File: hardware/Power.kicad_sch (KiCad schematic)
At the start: 28 parts, among them J1 DC Connector, Q1 DMP6180SK3-13, U1 AP66200

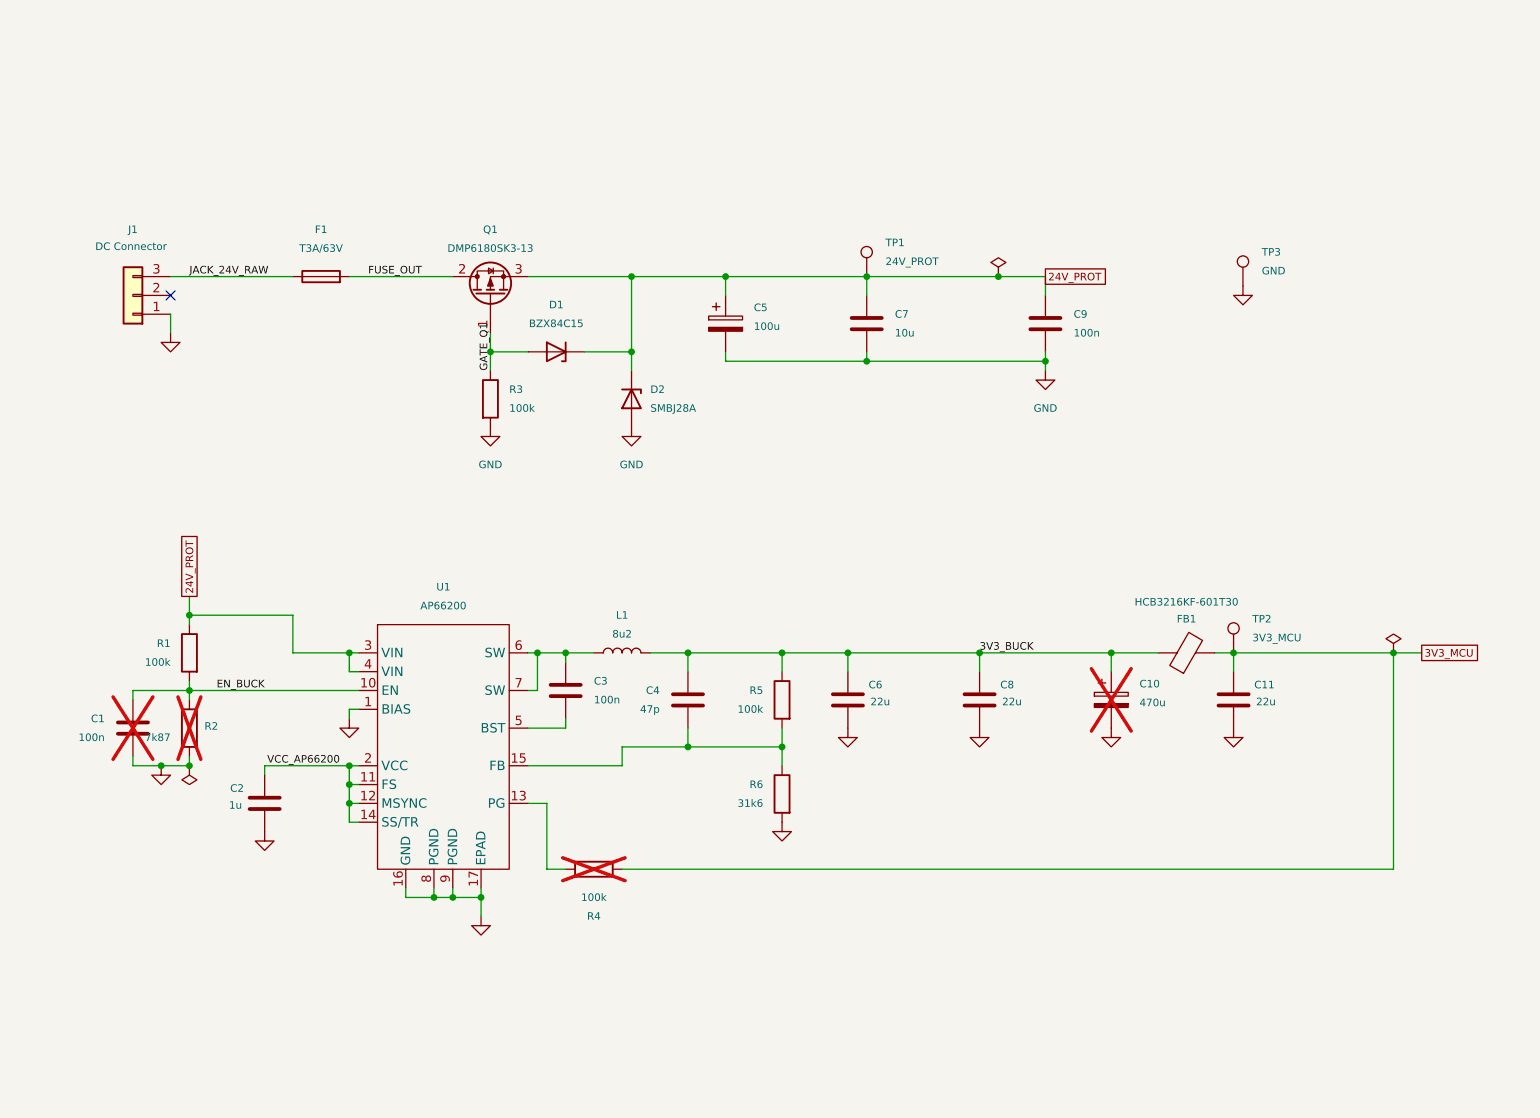
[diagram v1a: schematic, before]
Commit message: Updated power schematic, delated buck schematic
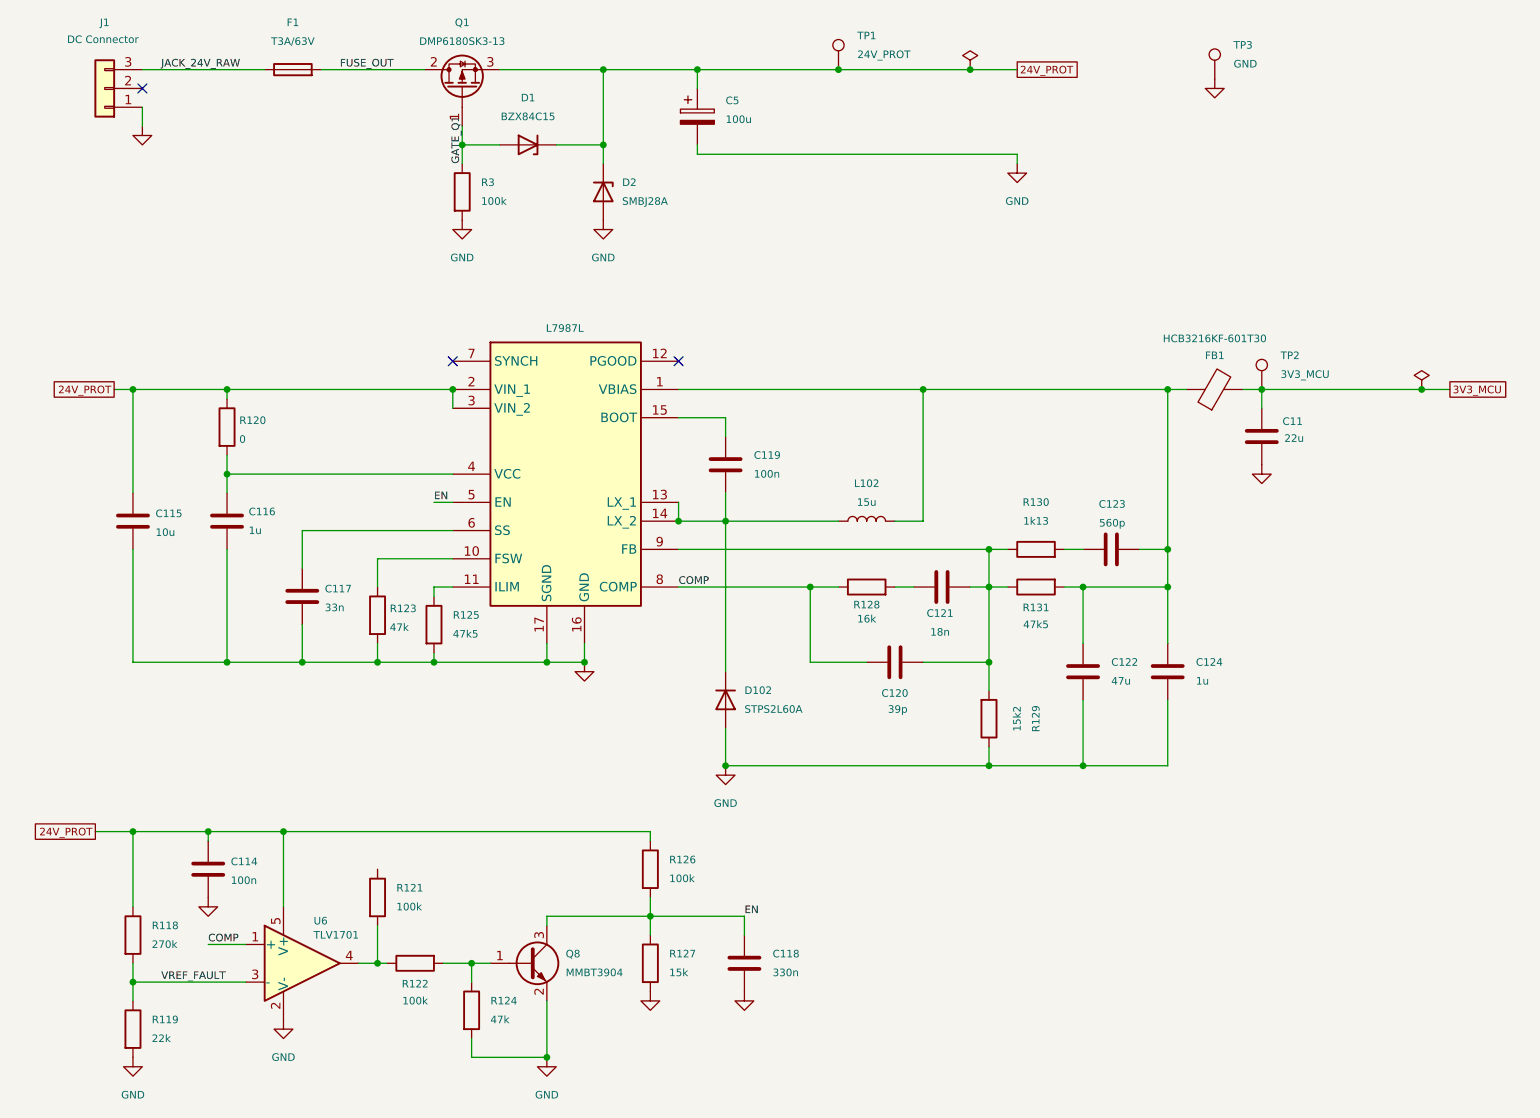
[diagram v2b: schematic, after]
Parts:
- removed C1, C3, C9: 100n, Capacitor_SMD:C_0603_1608Metric, symbol Device:C
- removed C10: 470u, Capacitor_SMD:CP_Elec_8x10, symbol Device:C_Polarized
- removed C2: 1u, Capacitor_SMD:C_0603_1608Metric, symbol Device:C
- removed C4: 47p, Capacitor_SMD:C_0603_1608Metric, symbol Device:C
- removed C6, C8: 22u, Capacitor_SMD:C_0805_2012Metric, symbol Device:C
- removed C7: 10u, Capacitor_SMD:C_1210_3225Metric, symbol Device:C
- removed L1: 8u2, JLCPCB:IND-SMD_L7.0-W6.6_ZD0650-100M, symbol Device:L
- removed R1, R4, R5: 100k, Resistor_SMD:R_0603_1608Metric, symbol Device:R
- removed R2: 7k87, Resistor_SMD:R_0603_1608Metric, symbol Device:R
- removed R6: 31k6, Resistor_SMD:R_0603_1608Metric, symbol Device:R
- removed U1: AP66200, FilamentDryer:AP66200_U-QFN4040-16_EP2.6x2.6mm_P0.65mm, symbol Filament_Dryer_Custom:AP66200
- added C114, C119: 100n, symbol Device:C
- added C115: 10u, symbol Device:C
- added C116, C124: 1u, symbol Device:C
- added C117: 33n, symbol Device:C
- added C118: 330n, symbol Device:C
- added C120: 39p, symbol Device:C
- added C121: 18n, symbol Device:C
- added C122: 47u, symbol Device:C
- added C123: 560p, symbol Device:C
- added D102: STPS2L60A, symbol Device:D
- added L102: 15u, symbol Device:L
- added Q8: MMBT3904, Package_TO_SOT_SMD:SOT-23, symbol Transistor_BJT:Q_NPN_BEC
- added R118: 270k, symbol Device:R
- added R119: 22k, symbol Device:R
- added R120: 0, symbol Device:R
- added R121, R122, R126: 100k, symbol Device:R
- added R123, R124: 47k, symbol Device:R
- added R125, R131: 47k5, symbol Device:R
- added R127: 15k, symbol Device:R
- added R128: 16k, symbol Device:R
- added R129: 15k2, symbol Device:R
- added R130: 1k13, symbol Device:R
- added U102: L7987L, SOP65P640X120-17N, symbol SamacSys_Parts:L7987L
- added U6: TLV1701, Package_TO_SOT_SMD:SOT-23-5, symbol Filament_Dryer_Custom:TLV1701AIDBVR
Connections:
- net 24V_PROT: now also C114.1, C115.1, R118.1, R120.1, R126.1, U102.2 (VIN_1), U102.3 (VIN_2), U6.5 (V+)
- net GND: now also C114.2, C115.2, C116.2, C117.2, C118.2, C122.2, C124.2, D102.2 (A), Q8.2 (E), R119.2, R123.2, R124.2, R125.2, R127.2, R129.1, U102.16 (GND), U102.17 (SGND), U6.2 (V-)
- net 3V3_BUCK: no longer names the net of FB1.1
- net 3V3_BUCK: now also C122.1, C123.2, C124.1, L102.2, R131.2, U102.1 (VBIAS)
- new net: C123.1, R130.2
- new net: Q8.1 (B), R122.2, R124.1
- new net: C121.1, R128.2
- new net: C120.2, C121.2, R129.2, R130.1, R131.1, U102.9 (FB)
- new net: R125.1, U102.11 (ILIM)
- new net: C119.1, U102.15 (BOOT)
- new net: C119.2, D102.1 (K), L102.1, U102.13 (LX_1), U102.14 (LX_2)
- new net: C116.1, R120.2, U102.4 (VCC)
- new net: R123.1, U102.10 (FSW)
- new net: C117.1, U102.6 (SS)
- new net: R121.2, R122.1, U6.4
- new net COMP: C120.1, R128.1, U102.8 (COMP), U6.1 (+)
- new net EN: C118.1, Q8.3 (C), R126.2, R127.1, U102.5 (EN)
- new net VREF_FAULT: R118.2, R119.1, U6.3 (-)
- no-connect marks 1 -> 3
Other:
- moved on the sheet: C11, C5, D1, D2, F1, FB1, J1, Q1, R3, TP1, TP2, TP3

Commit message: Updated buck circuit references
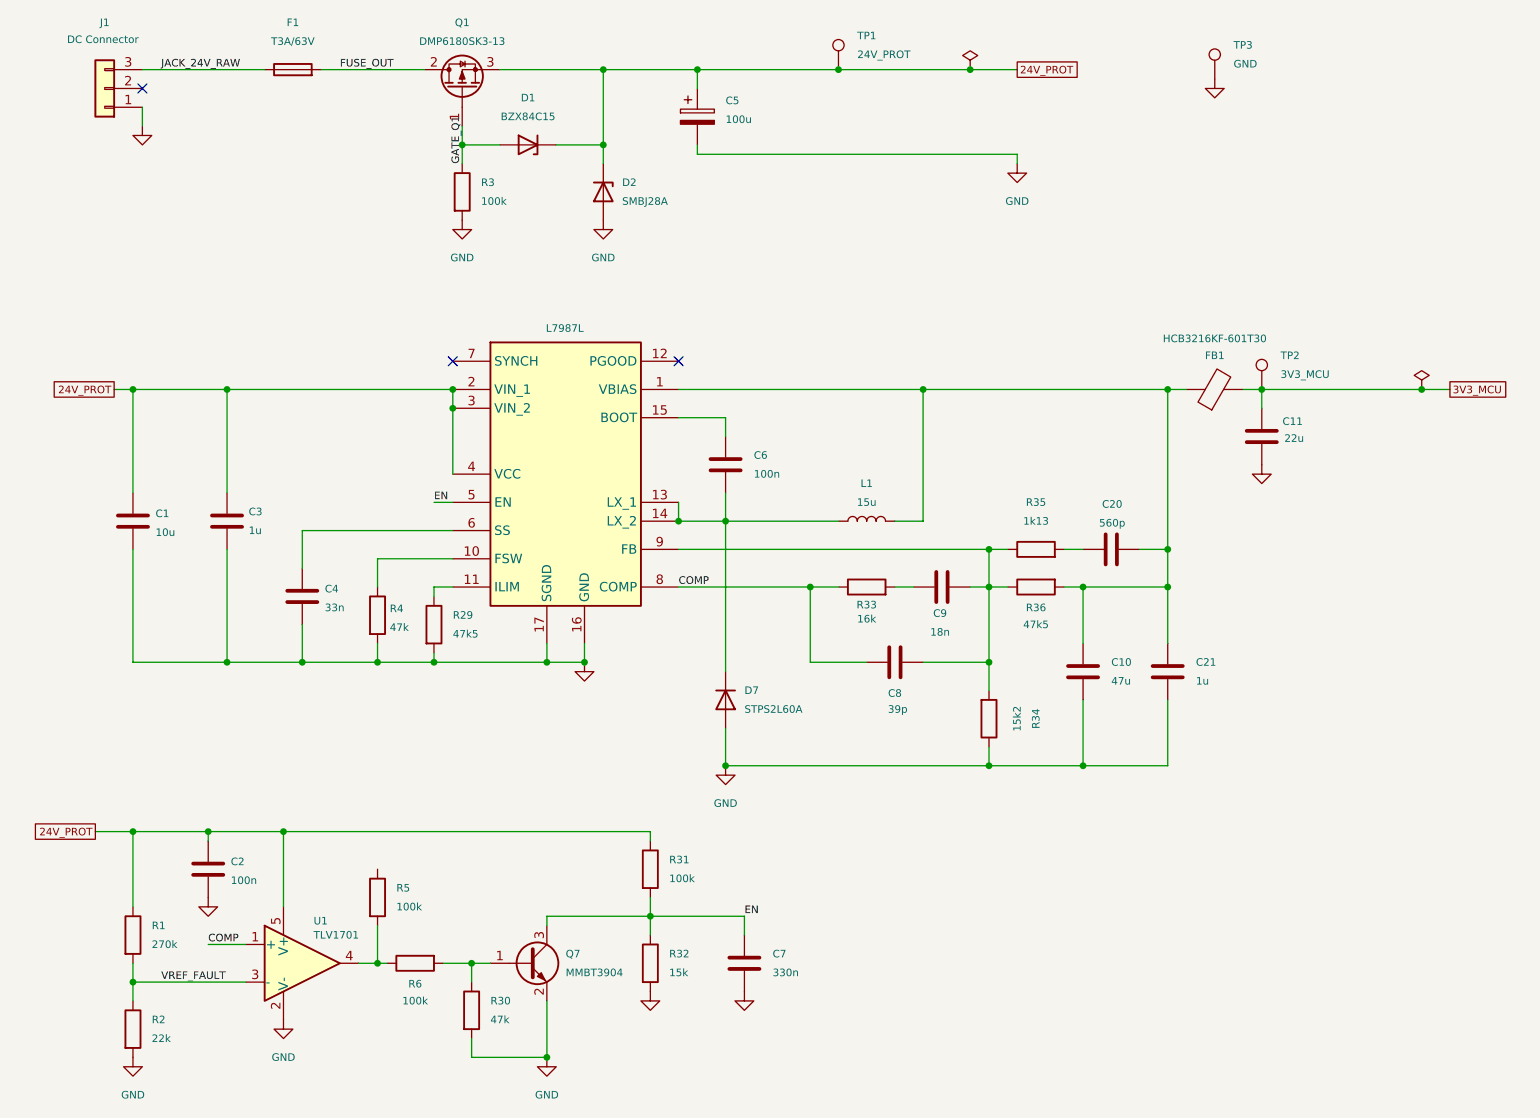
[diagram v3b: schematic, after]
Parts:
- removed R120: 0, symbol Device:R
- renumbered C115 to C1, C122 to C10, C114 to C2, C123 to C20, C124 to C21, C116 to C3, C117 to C4, C119 to C6, C118 to C7, C120 to C8, C121 to C9, D102 to D7, L102 to L1, Q8 to Q7, R118 to R1, R119 to R2, R125 to R29, R124 to R30, R126 to R31, R127 to R32, R128 to R33, R129 to R34, R130 to R35, R131 to R36, R123 to R4, R121 to R5, R122 to R6, U6 to U1, U102 to U5
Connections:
- net 24V_PROT: now also C3.1, U5.4 (VCC)

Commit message: Netlist
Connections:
- net 24V_PROT: now also R5.1
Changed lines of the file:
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@@
+	)
+	(junction
+		(at 97.79 138.43)
+		(diameter 0)
+		(color 0 0 0 0)
 	)
 	(junction
@@
 	(wire
 		(pts
+			(xy 97.79 143.51) (xy 97.79 138.43)
+		)
+		(stroke
+			(width 0)
+			(type default)
+		)
+	)
+	(wire
+		(pts
 			(xy 217.17 78.74) (xy 214.63 78.74)
 		)
@@
 	(wire
 		(pts
+			(xy 97.79 138.43) (xy 134.62 138.43)
+		)
+		(stroke
+			(width 0)
+			(type default)
+		)
+	)
+	(wire
+		(pts
 			(xy 156.21 115.57) (xy 156.21 105.41)
 		)
@@
 	(wire
 		(pts
-			(xy 85.09 138.43) (xy 134.62 138.43)
-		)
-		(stroke
+			(xy 85.09 138.43) (xy 97.79 138.43)
+		)
+		(stroke

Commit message: Add buzzer transistor base pull-down
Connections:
- net 3V3_BUCK: now reaches C10.1, C20.2, C21.1, FB1.1, L1.2, R36.2, U5.1 (VBIAS)
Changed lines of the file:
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@@
 		)
 	)
+	(label "3V3_BUCK"
+		(at 144.78 78.74 0)
+		(effects
+			(font
+				(size 1.016 1.016)
+			)
+			(justify left bottom)
+		)
+	)
 	(label "JACK_24V_RAW"
 		(at 68.58 35.56 0)
@@
 			)
 		)
-		(property "Datasheet" "http://www.ti.com/lit/ds/symlink/lm397.pdf"
+		(property "Datasheet" "https://www.ti.com/lit/ds/symlink/tlv1701.pdf"
 			(at 87.63 151.13 0)
 			(hide yes)

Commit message: Sync KiCad component metadata with TME BOM
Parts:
- C1: Dielectric (none) -> X7S; Function (none) -> Cin_buck1; Manufacturer Murata -> MURATA; Tolerance (none) -> 10%; Voltage (none) -> 100V
- C10: Dielectric (none) -> X7R; Function (none) -> Cout_buck1; MPN EMK325BJ476MM-P, -> LMK325B7476KM-PR; Manufacturer Taiyo Yuden -> TAIYO YUDEN; Tolerance (none) -> 10%; Voltage (none) -> 10V
- C11: LCSC C45783 -> (none); MPN CL21A226MAQNNNE -> CL21A226MAYNNNE; Manufacturer Samsung -> SAMSUNG
- C2: Dielectric (none) -> X7R; Function (none) -> C_autoen_vdd1; MPN (none) -> CC0603KRX7R9BB104; Manufacturer (none) -> YAGEO; Tolerance (none) -> 10%; Voltage (none) -> 50V
- C20: Dielectric (none) -> C0G/NP0; Function (none) -> C_comp_cs1; MPN (none) -> 06035A561JAT2A; Manufacturer (none) -> KYOCERA AVX; Tolerance (none) -> 5%; Voltage (none) -> 50V
- C21: Dielectric (none) -> X7R; Function (none) -> C_vbias1; MPN GRJ21BC72A105KE11L -> GCM188R71E105KA64J; Manufacturer Murata -> MURATA; Tolerance (none) -> 10%; Voltage (none) -> 25V
- C3: Dielectric (none) -> X7S; Function (none) -> C_vcc_buck1; Manufacturer Murata -> MURATA; Tolerance (none) -> 10%; Voltage (none) -> 100V
- C4: Dielectric (none) -> X7R; Function (none) -> C_ss1; MPN (none) -> GCM188R71H333KA55D; Manufacturer (none) -> MURATA; Tolerance (none) -> 10%; Voltage (none) -> 50V
- C5: LCSC C401753 -> (none); MPN EEEFP1H101AP -> EEEFK1H101P; Manufacturer Panasonic -> PANASONIC
- C6: Dielectric (none) -> X7R; Function (none) -> Cbst1; MPN (none) -> CC0603KRX7R9BB104; Manufacturer (none) -> YAGEO; Tolerance (none) -> 10%; Voltage (none) -> 50V
- C7: Dielectric (none) -> X7R; Function (none) -> C_en_timing1; MPN (none) -> GRM219R71H334KA88D; Manufacturer (none) -> MURATA; Tolerance (none) -> 10%; Voltage (none) -> 50V
- C8: Dielectric (none) -> C0G/NP0; Function (none) -> C_comp_cp1; MPN (none) -> C0603C390J5GACTU; Manufacturer (none) -> KEMET; Tolerance (none) -> 5%; Voltage (none) -> 50V
- C9: Dielectric (none) -> C0G/NP0; Function (none) -> C_comp_cf1; MPN (none) -> GRM21B5C1H183JA01L; Manufacturer (none) -> MURATA; Tolerance (none) -> 5%; Voltage (none) -> 50V
- D1: LCSC C500789 -> (none); Manufacturer Diodes Incorporated -> DIODES INCORPORATED
- D2: LCSC C96335 -> (none); MPN SMBJ28A-TR -> SMBJ28A; Manufacturer STMicroelectronics -> LITTELFUSE
- D7: Function (none) -> D_buck1; Manufacturer STMicroelectronics -> STMicroelectronics
- F1: LCSC C354897 -> (none); MPN 1206T3A63V -> 0685T3000-01; Manufacturer Walter Elec -> BEL FUSE
- FB1: LCSC C357023 -> (none); MPN HCB3216KF-601T30 -> BLM31KN601SH1L; Manufacturer TAI-TECH -> MURATA
- J1: LCSC C144394 -> (none); MPN B3B-XH-A(LF)(SN) -> B3B-XH-A (LF)(SN)
- L1: Function (none) -> L_buck1
- Q1: LCSC C93034 -> (none); MPN DMP6180SK3-13 -> NTD20P06LT4G; Manufacturer Diodes Incorporated -> ONSEMI
- Q7: Function Q_boot1 -> Q_autoen1; LCSC C94514 -> (none); MPN MMBT3904-7-F -> MMBT3904; Manufacturer Diodes Incorporated -> DIOTEC SEMICONDUCTOR
- R1: Function (none) -> R_vref_top1; MPN (none) -> RC0603FR-07270KL; Manufacturer (none) -> YAGEO; Power (none) -> 100mW; TCR (none) -> 100ppm/K; Tolerance (none) -> 1%; Voltage (none) -> 75V
- R2: Function (none) -> R_vref_bot1; MPN (none) -> RC0603FR-0722KL; Manufacturer (none) -> YAGEO; Power (none) -> 100mW; TCR (none) -> 100ppm/K; Tolerance (none) -> 1%; Voltage (none) -> 75V
- R29: Function (none) -> R_ilim1; MPN (none) -> RC0603FR-0747K5L; Manufacturer (none) -> YAGEO; Power (none) -> 100mW; TCR (none) -> 100ppm/K; Tolerance (none) -> 1%; Voltage (none) -> 75V
- R3: LCSC C25803 -> (none); MPN 0603WAF1003T5E -> RC0603FR-07100KL; Manufacturer UNI-ROYAL(Uniroyal Elec) -> YAGEO; Voltage (none) -> 75V
- R30: Function (none) -> R_q7_pd1; MPN (none) -> RC0603FR-0747KL; Manufacturer (none) -> YAGEO; Power (none) -> 100mW; TCR (none) -> 100ppm/K; Tolerance (none) -> 1%; Voltage (none) -> 75V
- R31: Function (none) -> R_en_pu1; MPN (none) -> RC0603FR-07100KL; Manufacturer (none) -> YAGEO; Power (none) -> 100mW; TCR (none) -> 100ppm/K; Tolerance (none) -> 1%; Voltage (none) -> 75V
- R32: Function (none) -> R_en_pd1; MPN (none) -> RC0603FR-0715KL; Manufacturer (none) -> YAGEO; Power (none) -> 100mW; TCR (none) -> 100ppm/K; Tolerance (none) -> 1%; Voltage (none) -> 75V
- R33: Function (none) -> R_comp_rf1; MPN (none) -> RC0603FR-0716KL; Manufacturer (none) -> YAGEO; Power (none) -> 100mW; TCR (none) -> 100ppm/K; Tolerance (none) -> 1%; Voltage (none) -> 75V
- R34: Function (none) -> Rfb_bot1
- R35: Function (none) -> R_comp_rs1; MPN (none) -> ERA3AEB1131V; Manufacturer (none) -> PANASONIC; Power (none) -> 100mW; TCR (none) -> 25ppm/K; Tolerance (none) -> 0.1%; Voltage (none) -> 75V
- R36: Function (none) -> Rfb_top1
- R4: Function (none) -> R_fsw1; MPN (none) -> RC0603FR-0747KL; Manufacturer (none) -> YAGEO; Power (none) -> 100mW; TCR (none) -> 100ppm/K; Tolerance (none) -> 1%; Voltage (none) -> 75V
- R5: Function (none) -> R_cmp_pu1; MPN (none) -> RC0603FR-07100KL; Manufacturer (none) -> YAGEO; Power (none) -> 100mW; TCR (none) -> 100ppm/K; Tolerance (none) -> 1%; Voltage (none) -> 75V
- R6: Function (none) -> R_q_autoen1; MPN (none) -> RC0603FR-07100KL; Manufacturer (none) -> YAGEO; Power (none) -> 100mW; TCR (none) -> 100ppm/K; Tolerance (none) -> 1%; Voltage (none) -> 75V
- U1: Function (none) -> U_autoen_cmp1; MPN (none) -> TLV1701AIDBVR; Manufacturer (none) -> TEXAS INSTRUMENTS
- U5: Function (none) -> U_buck1; MPN (none) -> L7987L; Manufacturer (none) -> STMicroelectronics; Manufacturer_Name STMicroelectronics -> (none); Manufacturer_Part_Number L7987L -> (none)

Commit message: Updated R344 and R36 values
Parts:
- R34: value 15k2 -> 16k; MPN (none) -> RC0603FR-0716KL; Manufacturer (none) -> YAGEO; Power (none) -> 100mW; TCR (none) -> 100ppm/K; Tolerance (none) -> 1%; Voltage (none) -> 75V
- R36: value 47k5 -> 49k9; MPN (none) -> RC0603FR-0749K9L; Manufacturer (none) -> YAGEO; Power (none) -> 100mW; TCR (none) -> 100ppm/K; Tolerance (none) -> 1%; Voltage (none) -> 75V
